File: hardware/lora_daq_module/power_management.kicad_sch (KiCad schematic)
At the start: 0 parts

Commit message: added the mcp73833
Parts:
- added BT1: Single Li-Ion cell, symbol Device:Battery_Cell
- added C1, C2: 1uF, symbol Device:C_Small
- added D1, D2, D3: ~, symbol Device:LED
- added J1: USB_B_Mini, symbol Connector:USB_B_Mini
- added R1, R2, R3: 470Ω, symbol Device:R_US
- added R4, R5: 1kΩ, symbol Device:R_US
- added R6: 10kΩ, symbol Device:R_US
- added R7: 150kΩ, symbol Device:R_US
- added U1: MCP73833, Package_SO:MSOP-10_3x3mm_P0.5mm, symbol Battery_Management:MCP73833-xxx-UN
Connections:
- new net: R5.1, U1.8 (THERM)
- new net: R5.2, R6.1, R7.2
- new net: D3.1 (K), R3.1
- new net: R3.2, U1.3 (STAT1)
- new net: BT1.1 (+), C2.1, U1.10 (V_{BAT}), U1.9 (V_{BAT})
- new net: D2.1 (K), R2.1
- new net: R2.2, U1.4 (STAT2)
- new net: R4.2, U1.6 (PROG)
- new net: R1.2, U1.7 (~{PG})
- new net: D1.1 (K), R1.1
- new net +5V: J1.1 (VBUS)
- new net GND: BT1.2 (-), C1.2, C2.2, J1.5 (GND), R4.1, R6.2, R7.1, U1.5 (V_{SS})
- new net V_USB: C1.1, D1.2 (A), D2.2 (A), D3.2 (A), U1.1 (V_{DD}), U1.2 (V_{DD})
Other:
- title: (none) -> Power management schematic

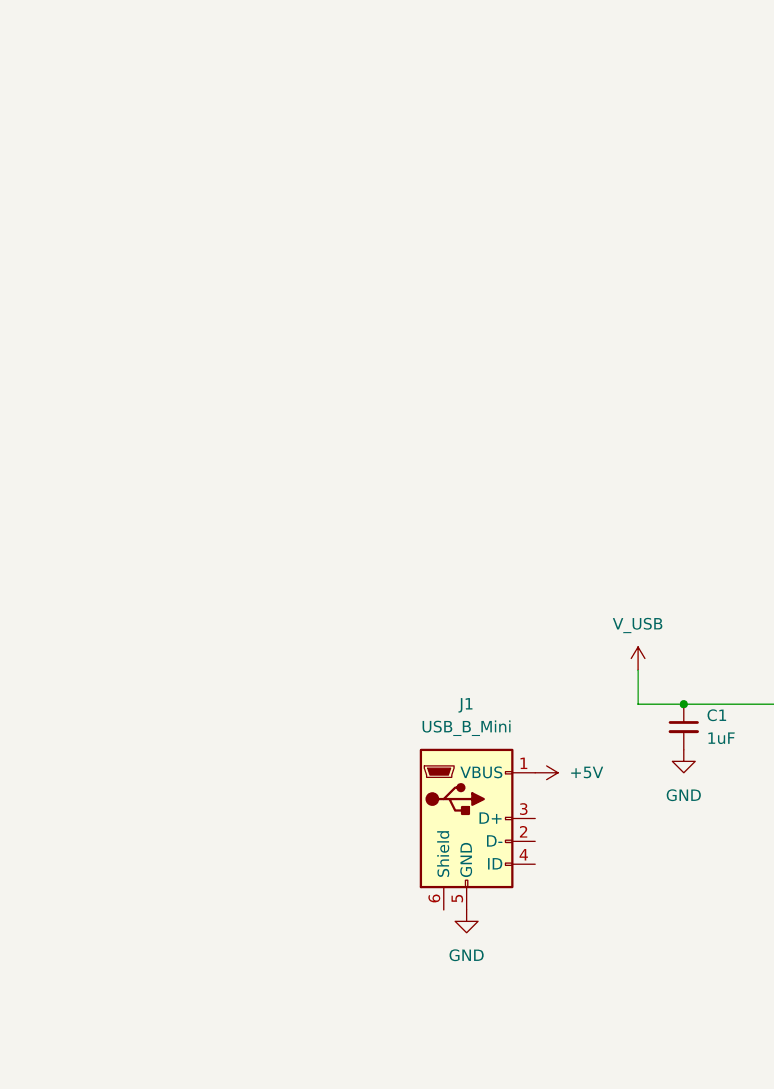
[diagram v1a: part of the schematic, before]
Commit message: added the tps63001 and tps63002 with their reference design
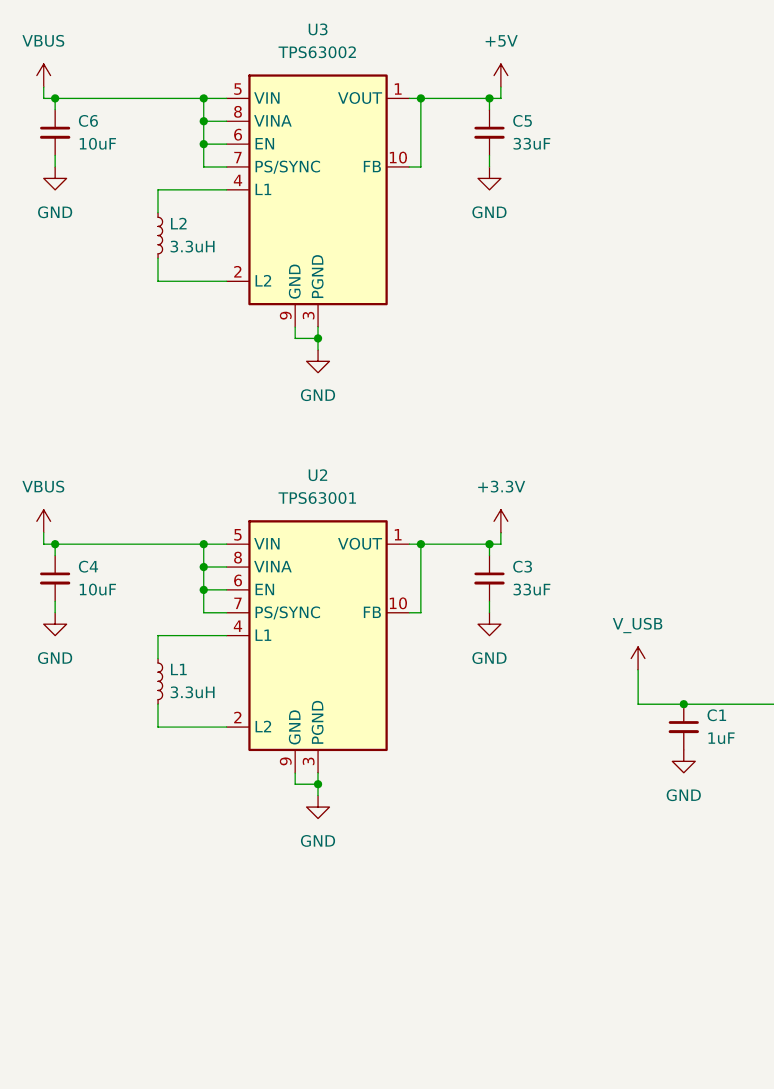
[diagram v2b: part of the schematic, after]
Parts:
- removed J1: USB_B_Mini, symbol Connector:USB_B_Mini
- added C3, C5: 33uF, symbol Device:C_Small
- added C4, C6: 10uF, symbol Device:C_Small
- added L1, L2: 3.3uH, symbol Device:L_Small
- added U2: TPS63001, Package_SON:Texas_DRC0010J_ThermalVias, symbol Regulator_Switching:TPS63001
- added U3: TPS63002, Package_SON:Texas_DRC0010J_ThermalVias, symbol Regulator_Switching:TPS63002
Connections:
- net +5V: now also C5.1, U3.1 (VOUT), U3.10 (FB)
- net GND: now also C3.2, C4.2, C5.2, C6.2, U2.11 (PGND), U2.3 (PGND), U2.9 (GND), U3.11 (PGND), U3.3 (PGND), U3.9 (GND)
- new net: L2.2, U3.2 (L2)
- new net: L2.1, U3.4 (L1)
- new net: L1.2, U2.2 (L2)
- new net: L1.1, U2.4 (L1)
- new net +3.3V: C3.1, U2.1 (VOUT), U2.10 (FB)
- new net VBUS: C4.1, C6.1, U2.5 (VIN), U2.6 (EN), U2.7 (PS/SYNC), U2.8 (VINA), U3.5 (VIN), U3.6 (EN), U3.7 (PS/SYNC), U3.8 (VINA)

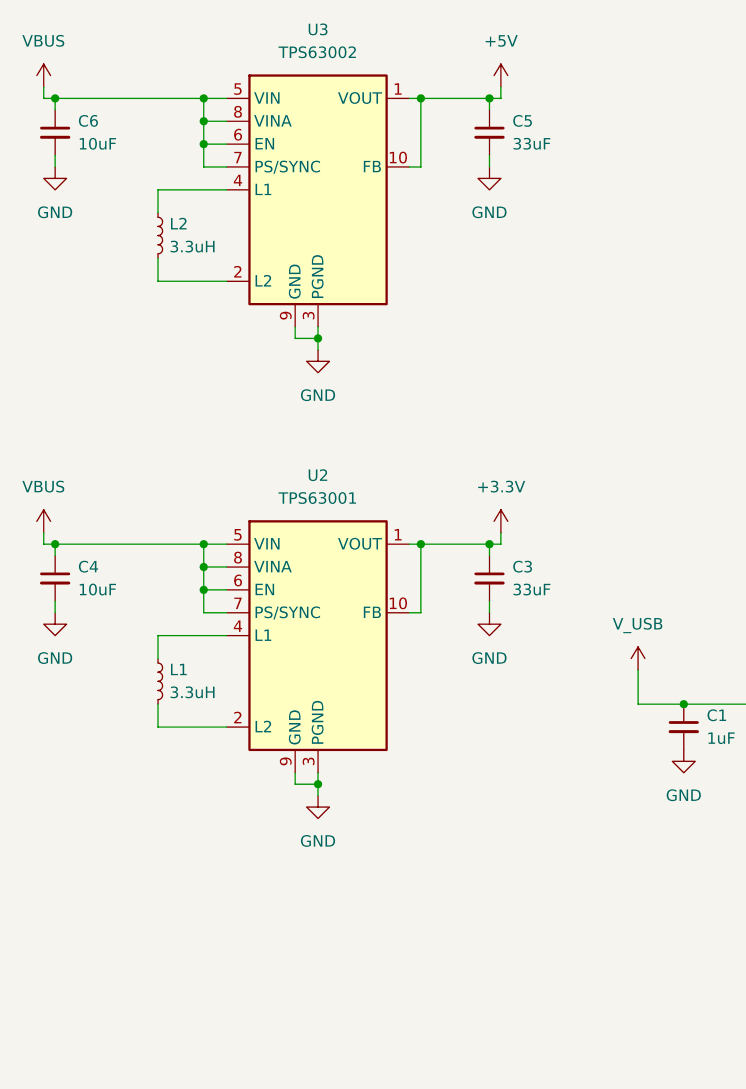
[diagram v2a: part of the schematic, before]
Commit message: Removed the 3.3V buck-boost converter from the original design, then added LDO
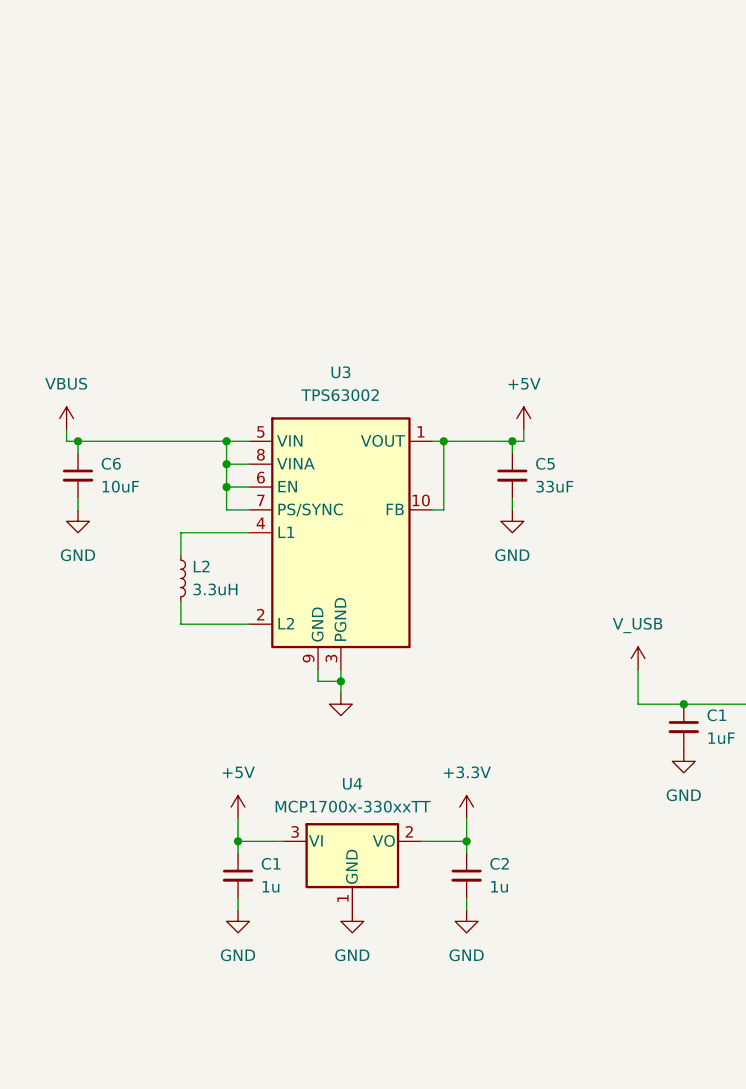
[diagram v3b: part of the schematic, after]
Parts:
- removed C3: 33uF, symbol Device:C_Small
- removed C4: 10uF, symbol Device:C_Small
- removed L1: 3.3uH, symbol Device:L_Small
- removed U2: TPS63001, Package_SON:Texas_DRC0010J_ThermalVias, symbol Regulator_Switching:TPS63001
- added C1, C2: 1u, symbol Device:C_Small
- added U4: MCP1700x-330xxTT, Package_TO_SOT_SMD:SOT-23, symbol Regulator_Linear:MCP1700x-330xxTT
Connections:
- net +3.3V: now also C2.1, U4.2 (VO)
- net +5V: now also C1.1, U4.3 (VI)
- net GND: now also C1.2, C2.2, U4.1 (GND)
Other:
- moved on the sheet: C5, C6, L2, U3

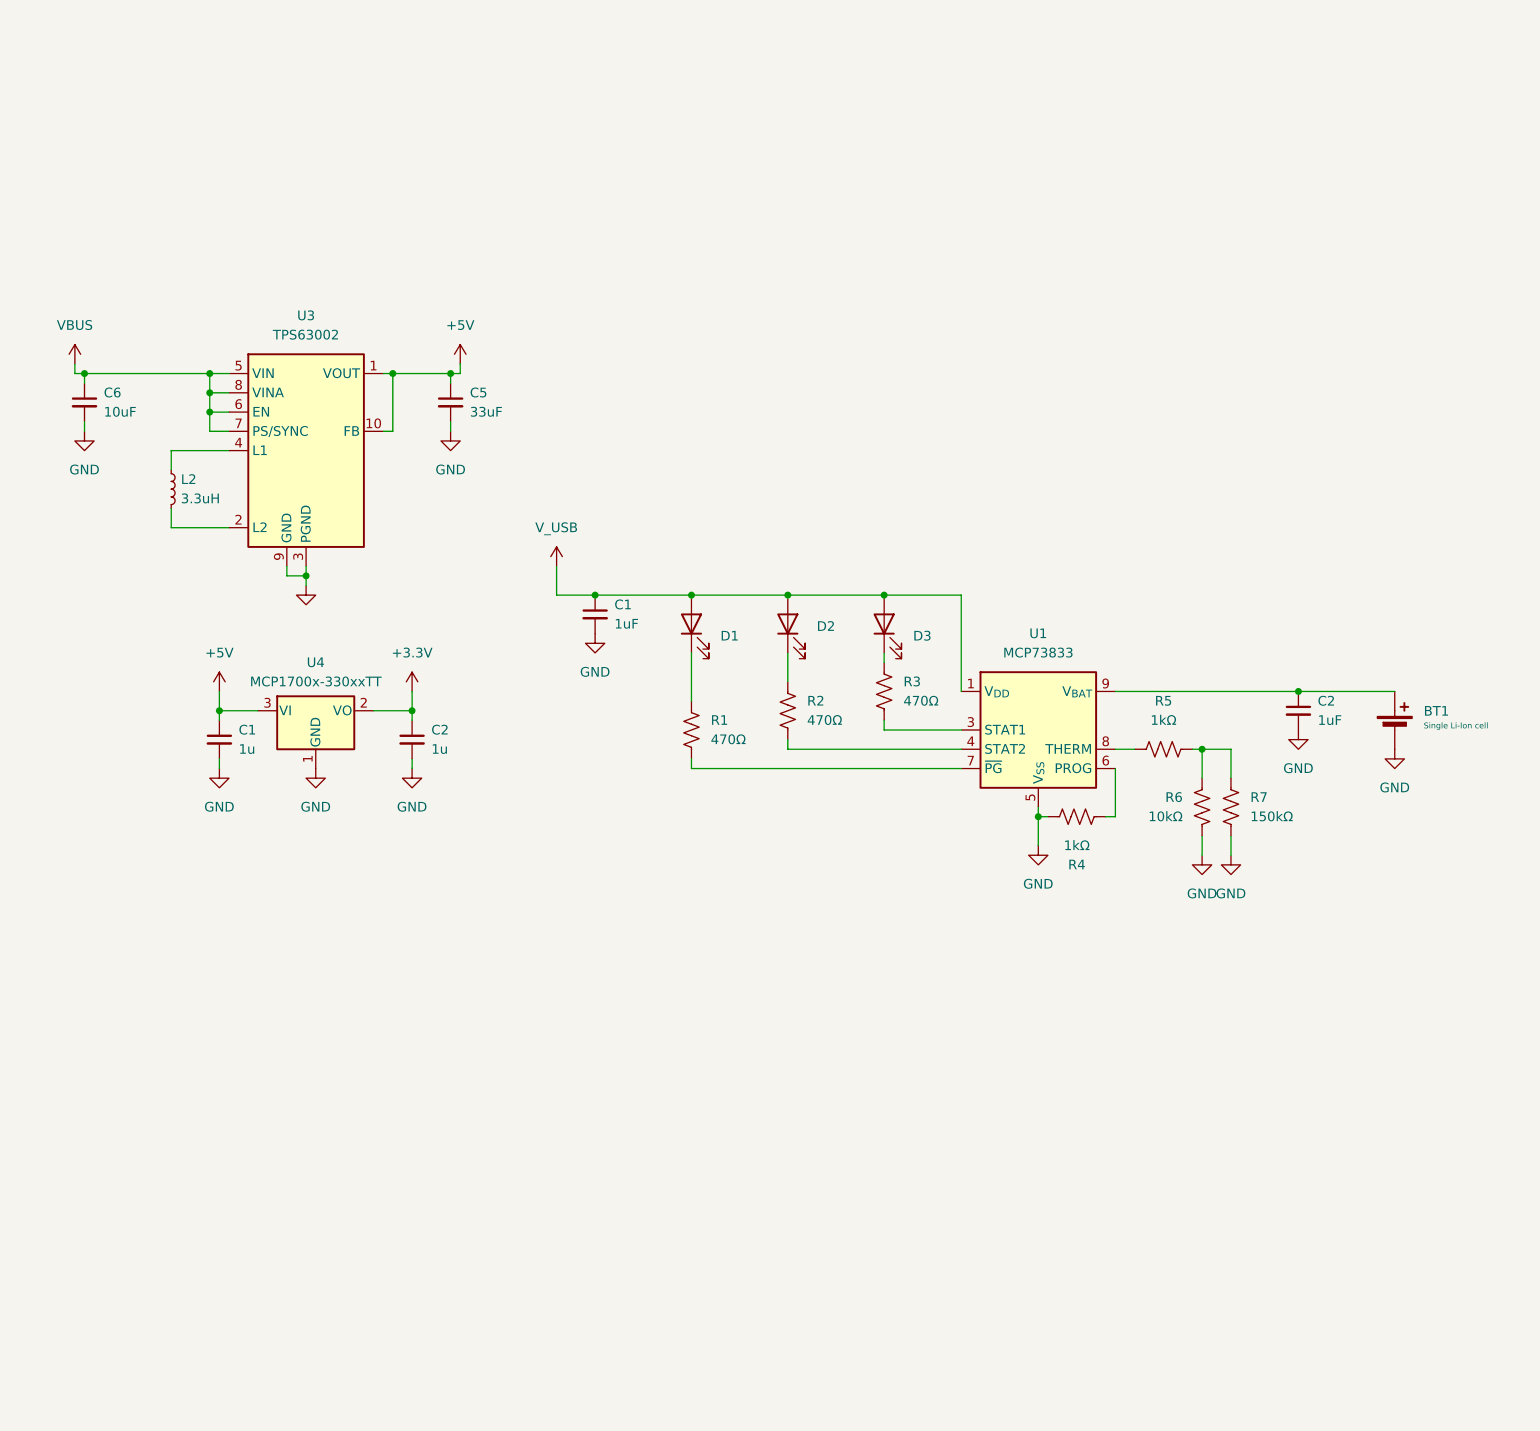
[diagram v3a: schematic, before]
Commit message: updated power schematic to include power switching IC for battery/usb power, minor changes to lora module schematic, added footprints to all component and began with the preliminary layout based on data sheet and application note reccomendations for each component.
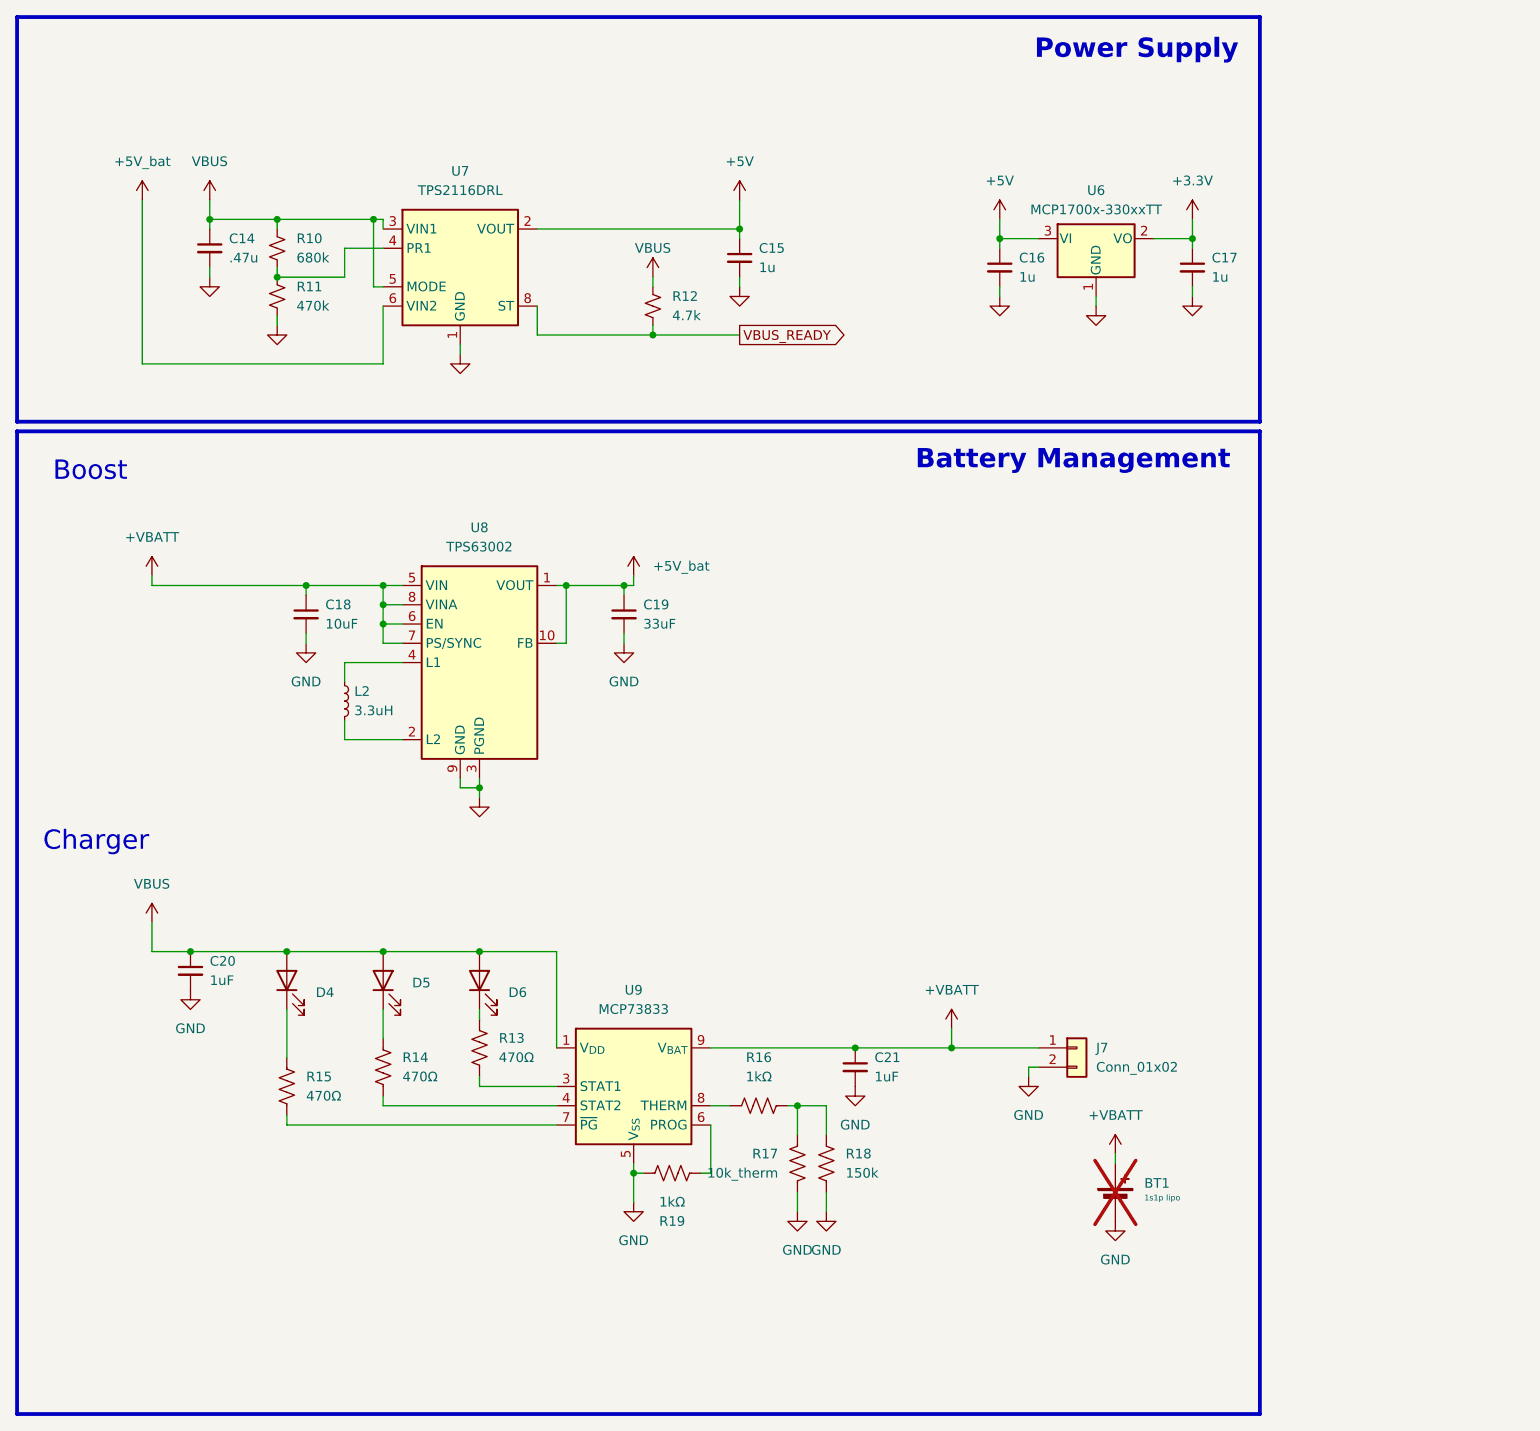
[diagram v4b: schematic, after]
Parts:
- added C14: .47u, Capacitor_SMD:C_0603_1608Metric, symbol Device:C_Small
- added C15: 1u, Capacitor_SMD:C_0603_1608Metric, symbol Device:C_Small
- added J7: Conn_01x02, Connector_PinHeader_2.54mm:PinHeader_1x02_P2.54mm_Vertical, symbol Connector_Generic:Conn_01x02
- added R10: 680k, Resistor_SMD:R_0603_1608Metric, symbol Device:R_Small_US
- added R11: 470k, Resistor_SMD:R_0603_1608Metric, symbol Device:R_Small_US
- added R12: 4.7k, Resistor_SMD:R_0603_1608Metric, symbol Device:R_Small_US
- added U7: TPS2116DRL, Package_TO_SOT_SMD:SOT-583-8, symbol Power_Management:TPS2116DRL
- BT1: value Single Li-Ion cell -> 1s1p lipo; now not fitted
- C16, C20: renamed from C1; footprint (none) -> Capacitor_SMD:C_0603_1608Metric
- C17, C21: renamed from C2; footprint (none) -> Capacitor_SMD:C_0603_1608Metric
- C18: renamed from C6; footprint (none) -> Capacitor_SMD:C_1206_3216Metric
- C19: renamed from C5; footprint (none) -> Capacitor_SMD:C_1210_3225Metric
- D4: renamed from D1; footprint (none) -> LED_SMD:LED_0603_1608Metric
- D5: renamed from D2; footprint (none) -> LED_SMD:LED_0603_1608Metric
- D6: renamed from D3; footprint (none) -> LED_SMD:LED_0603_1608Metric
- L2: footprint (none) -> Inductor_SMD:L_Coilcraft_LPS3010
- R13: renamed from R3; footprint (none) -> Resistor_SMD:R_0603_1608Metric
- R14: renamed from R2; footprint (none) -> Resistor_SMD:R_0603_1608Metric
- R15: renamed from R1; footprint (none) -> Resistor_SMD:R_0603_1608Metric
- R16: renamed from R5; footprint (none) -> Resistor_SMD:R_0603_1608Metric
- R17: renamed from R6; value 10kΩ -> 10k_therm; footprint (none) -> Resistor_SMD:R_0603_1608Metric
- R18: renamed from R7; value 150kΩ -> 150k; footprint (none) -> Resistor_SMD:R_0603_1608Metric
- R19: renamed from R4; footprint (none) -> Resistor_SMD:R_0603_1608Metric
- renumbered U4 to U6, U3 to U8, U1 to U9
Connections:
- net V_USB is gone; now on net VBUS: C20.1, D4.2 (A), D5.2 (A), D6.2 (A), U9.1 (V_{DD}), U9.2 (V_{DD})
- net +5V: now also C15.1, U7.2 (VOUT), U7.7 (VOUT); no longer C19.1, U8.1 (VOUT), U8.10 (FB)
- net GND: now also C14.2, C15.2, J7.2 (Pin_2), R11.2, U7.1 (GND)
- net VBUS: now also C14.1, R10.1, R12.1, U7.3 (VIN1), U7.5 (MODE); no longer C18.1, U8.5 (VIN), U8.6 (EN), U8.7 (PS/SYNC), U8.8 (VINA)
- net +VBATT: now reaches BT1.1 (+), C21.1, U9.10 (V_{BAT}), U9.9 (V_{BAT})
- net +VBATT: now also C18.1, U8.5 (VIN), U8.6 (EN), U8.7 (PS/SYNC), U8.8 (VINA), J7.1 (Pin_1)
- new net: R10.2, R11.1, U7.4 (PR1)
- new net +5V_bat: C19.1, U7.6 (VIN2), U8.1 (VOUT), U8.10 (FB)
- new net VBUS_READY: R12.2, U7.8 (ST)
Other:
- note added: "Battery Management"
- note added: "Boost"
- note added: "Charger"
- note added: "Power Supply"
- moved on the sheet: C16, C17, C18, C19, C20, C21, D4, D5, D6, L2, R13, R14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

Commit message: setup BOM columns
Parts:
- C14: value .47u -> 47n
- C18: value 10uF -> 10u
- C19: value 33uF -> 33u
- C20, C21: value 1uF -> 1u
- R13, R14, R15: value 470Ω -> 470
- R16, R19: value 1kΩ -> 1k
